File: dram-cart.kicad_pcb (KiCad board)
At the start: 2 copper layers, 67.9 x 32 mm, 7 parts, among them CON1 Conn_02x20_Odd_Even, U1 W25Q128JVSIQ, U2 IS42S16400J-xC

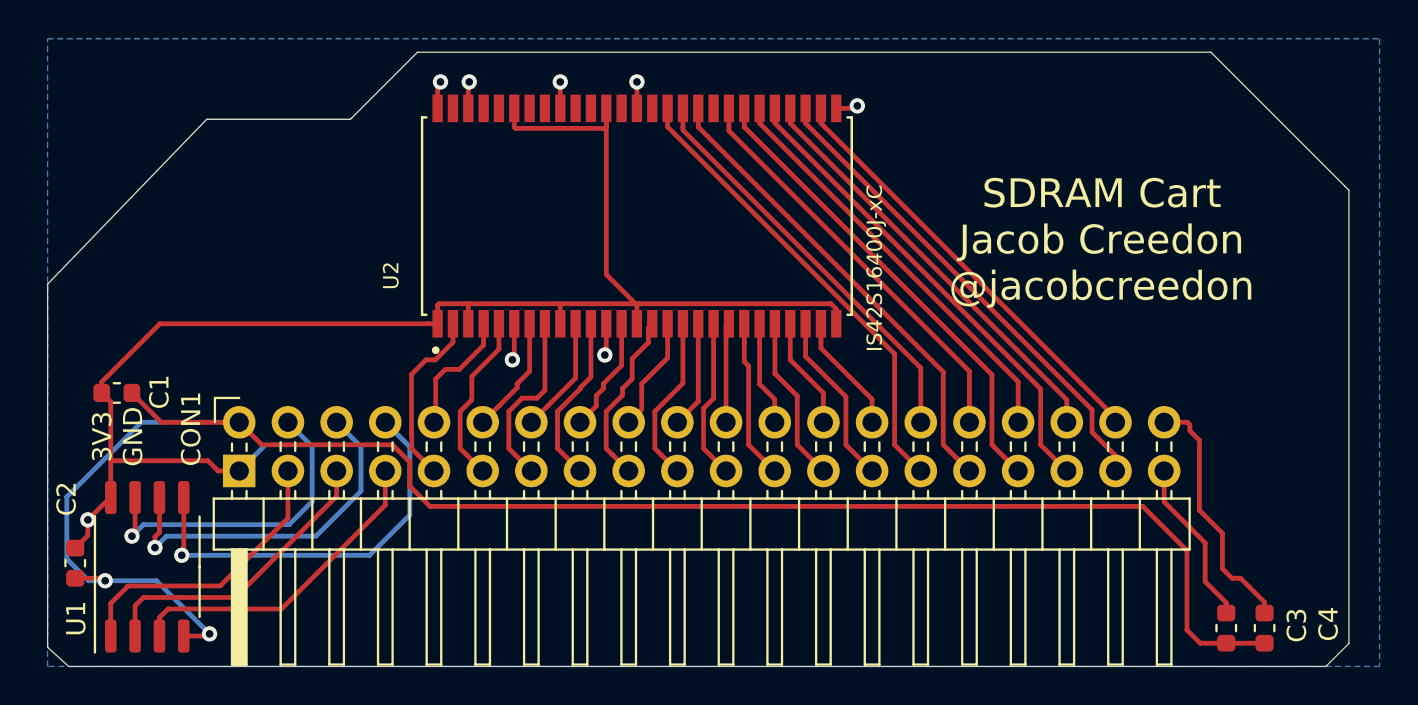
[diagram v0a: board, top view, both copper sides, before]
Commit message: Rev.B of Schematic and PCB
This corrects errors in Rev.A where the wrong pins were used for some DQ signals.

Signed-off-by: Jacob Creedon <jcreedon@gmail.com>
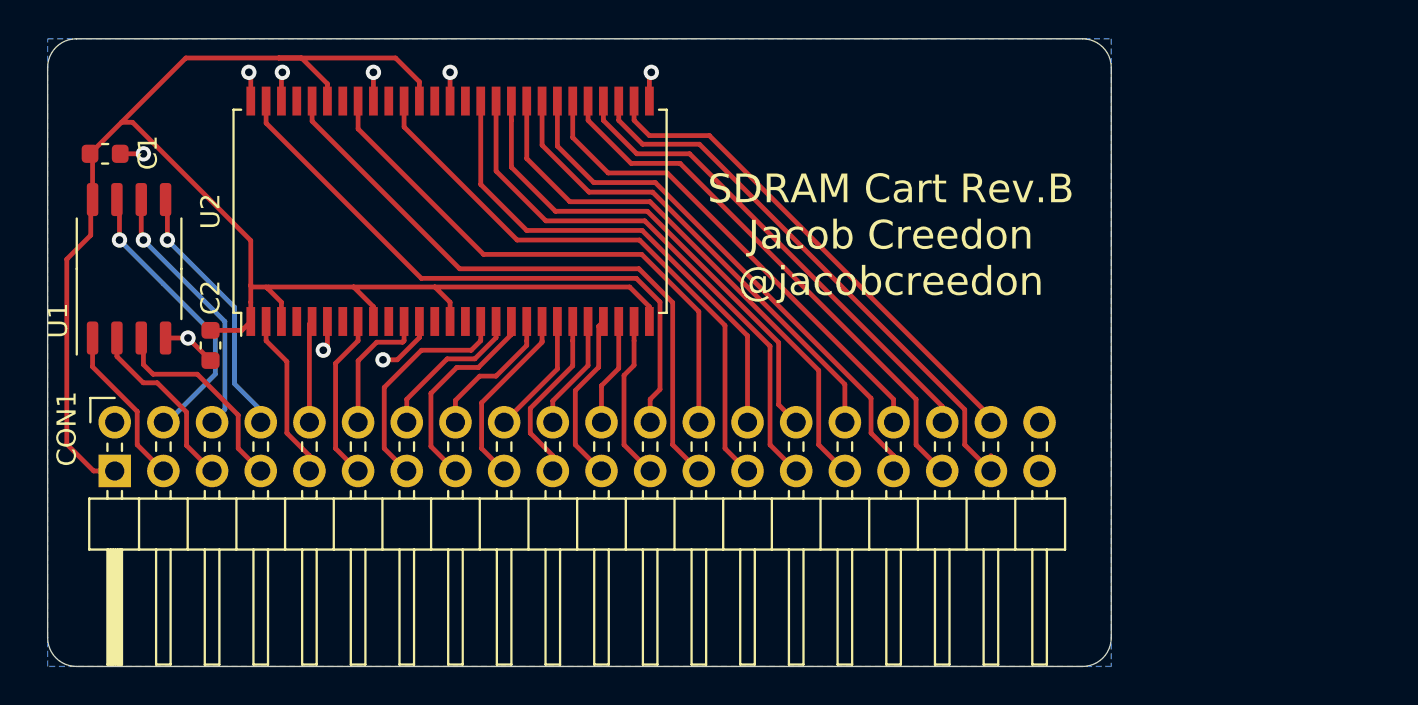
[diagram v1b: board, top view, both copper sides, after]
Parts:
- removed C3, C4: 100n, Capacitor_SMD:C_0603_1608Metric
- U2: value IS42S16400J-xC -> TSOP-II-54-x8; footprint IS42S16400J-6TL:SOP80P1176X120-54N -> Package_SO:TSOP-II-54_22.2x10.16mm_P0.8mm
- moved U1 15.6 mm to (106.2, 63.2)
- moved C2 13.4 mm to (110.5, 67.2)
- moved C1 12.5 mm to (105.0, 57.2)
- moved U2 9.75 mm to (123.0, 60.2)
- moved CON1 6.50 mm to (105.5, 73.8)
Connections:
- CON1 pad 39: VBAT -> (no net)
- CON1 pad 40: 5V -> (no net)
- U2 pad 10: GENIO6 -> (no net)
- U2 pad 11: GENIO7 -> GENIO4
- U2 pad 13: GENIO8 -> (no net)
- U2 pad 15: GENIO9 -> (no net)
- U2 pad 16: GENIO10 -> GENIO5
- U2 pad 17: GENIO11 -> GENIO6
- U2 pad 18: GENIO12 -> GENIO7
- U2 pad 19: GENIO13 -> GENIO8
- U2 pad 20: GENIO14 -> GENIO9
- U2 pad 21: GENIO15 -> GENIO10
- U2 pad 22: GENIO16 -> GENIO11
- U2 pad 23: GENIO17 -> GENIO12
- U2 pad 24: GENIO18 -> GENIO13
- U2 pad 25: GENIO19 -> GENIO14
- U2 pad 26: GENIO20 -> GENIO15
- U2 pad 36: (no net) -> GENIO23
- U2 pad 37: GENIO23 -> GENIO22
- U2 pad 38: GENIO22 -> GENIO21
- U2 pad 39: GENIO21 -> GENIO20
- U2 pad 4: GENIO2 -> (no net)
- U2 pad 44: (no net) -> GENIO19
- U2 pad 47: (no net) -> GENIO18
- U2 pad 5: GENIO3 -> GENIO2
- U2 pad 50: (no net) -> GENIO17
- U2 pad 53: (no net) -> GENIO16
- U2 pad 7: GENIO4 -> (no net)
- U2 pad 8: GENIO5 -> GENIO3
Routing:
- net GND: track 103.5 -> 16.5 mm
- net GENIO16: track 5.47 -> 32.1 mm
- net GENIO17: track 8.73 -> 33.1 mm
- net GENIO18: track 5.86 -> 29.0 mm
- net GENIO19: track 9.12 -> 30.5 mm
- net GENIO20: track 6.25 -> 26.1 mm
- net 5V: track 13.1 -> 0.00 mm
- net VBAT: track 8.75 -> 0.00 mm
- net 3V3: track 80.3 -> 87.9 mm, vias 1 -> 0
- net MOSI: track 21.2 -> 13.7 mm
- net CS: track 15.3 -> 8.47 mm
- net MISO: track 15.8 -> 9.42 mm
- net WP: track 17.0 -> 10.9 mm
- net SCK: track 18.8 -> 13.7 mm
- net GENIO21: track 24.4 -> 28.8 mm
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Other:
- board size 67.9 x 32 mm -> 55.5 x 32.8 mm
- board text added: "SDRAM Cart Rev.B Jacob Creedon @jacobcreedon"
- board text removed: "HDR1: 3V3 GND 3V3 GND 3V3 GND 3V3 GND IO1 IO2 IO3 IO4 IO5 IO6 .... IO29 IO30 5V VBAT"
- board text removed: "SDRAM Cart Jacob Creedon @jacobcreedon"
